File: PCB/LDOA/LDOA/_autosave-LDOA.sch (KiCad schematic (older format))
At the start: 41 parts, among them Q1 BC547, Q10 BS250, Q2 BC547, Q3 BC557, Q4 BC547, Q5 BC557, Q6 BC547, Q7 2N7000, Q8 IRF9520, Q9 BS250

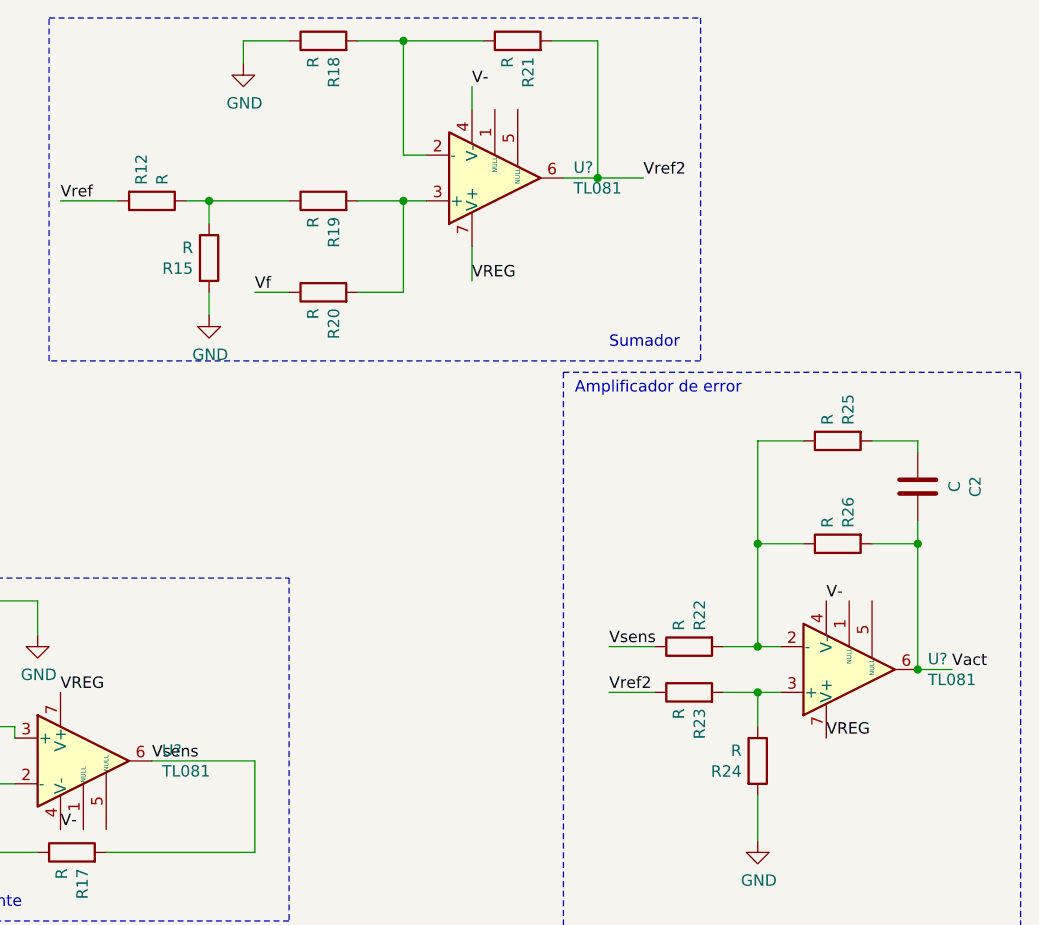
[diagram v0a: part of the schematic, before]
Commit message: Se agregaron más componentes al PCB. Hay que seguir trabajando con la distrubicion de los componentes
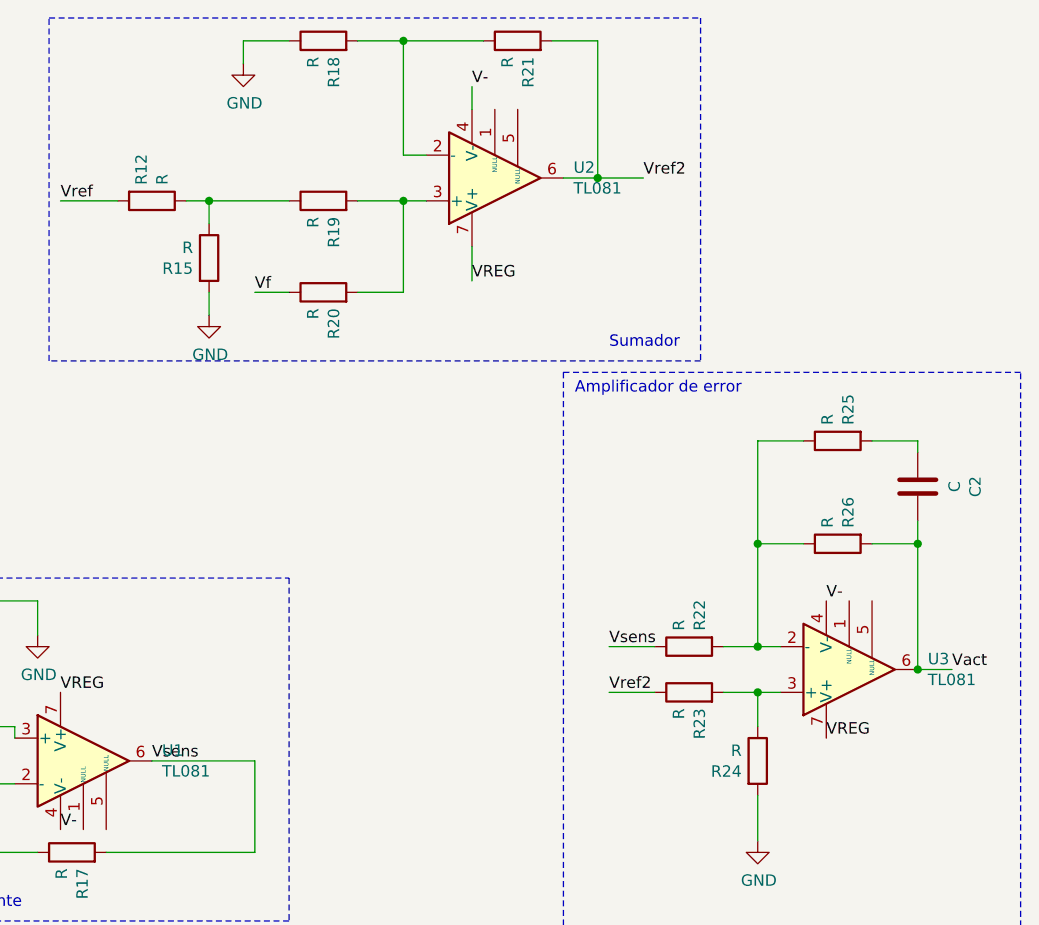
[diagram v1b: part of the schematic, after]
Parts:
- U1, U2, U3: renamed from U?; footprint (none) -> Package_DIP:DIP-8_W7.62mm
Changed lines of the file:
@@
 	1300 3700 1350 3700
 $Comp
-L Amplifier_Operational:TL081 U?
+L Amplifier_Operational:TL081 U1
 U 1 1 62A878D4
 P 6000 3750
-F 0 "U?" H 6344 3796 50  0000 L CNN
+F 0 "U1" H 6344 3796 50  0000 L CNN
 F 1 "TL081" H 6344 3705 50  0000 L CNN
-F 2 "" H 6050 3800 50  0001 C CNN
+F 2 "Package_DIP:DIP-8_W7.62mm" H 6050 3800 50  0001 C CNN
 F 3 "http://www.ti.com/lit/ds/symlink/tl081.pdf" H 6150 3900 50  0001 C CNN
 	1    6000 3750
@@
 V-
 $Comp
-L Amplifier_Operational:TL081 U?
+L Amplifier_Operational:TL081 U3
 U 1 1 62A8B621
 P 9350 3350
-F 0 "U?" H 9694 3304 50  0000 L CNN
+F 0 "U3" H 9694 3304 50  0000 L CNN
 F 1 "TL081" H 9694 3395 50  0000 L CNN
-F 2 "" H 9400 3400 50  0001 C CNN
+F 2 "Package_DIP:DIP-8_W7.62mm" H 9400 3400 50  0001 C CNN
 F 3 "http://www.ti.com/lit/ds/symlink/tl081.pdf" H 9500 3500 50  0001 C CNN
 	1    9350 3350
@@
 V-
 $Comp
-L Amplifier_Operational:TL081 U?
+L Amplifier_Operational:TL081 U2
 U 1 1 62A94557
 P 7800 1200
-F 0 "U?" H 8144 1154 50  0000 L CNN
+F 0 "U2" H 8144 1154 50  0000 L CNN
 F 1 "TL081" H 8144 1245 50  0000 L CNN
-F 2 "" H 7850 1250 50  0001 C CNN
+F 2 "Package_DIP:DIP-8_W7.62mm" H 7850 1250 50  0001 C CNN
 F 3 "http://www.ti.com/lit/ds/symlink/tl081.pdf" H 7950 1350 50  0001 C CNN
 	1    7800 1200
